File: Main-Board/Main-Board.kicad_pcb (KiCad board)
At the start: 2 copper layers, 50 x 50 mm, 68 parts, among them J1 Power_In, J2 ESC_1, J3 ESC_2, J4 ESC_3, J5 ESC_4, J6 Receiver, J7 Aux, J8 USB_B_Micro, J9 ICSP, Q1 BSS138, Q2 BSS138, SW1 Reset, U1 MCP6001U, U2 ICM-20689, U3 FT232RL, U4 ATmega328P-AU, U5 LM1117-5.0, Y1 16 MHz

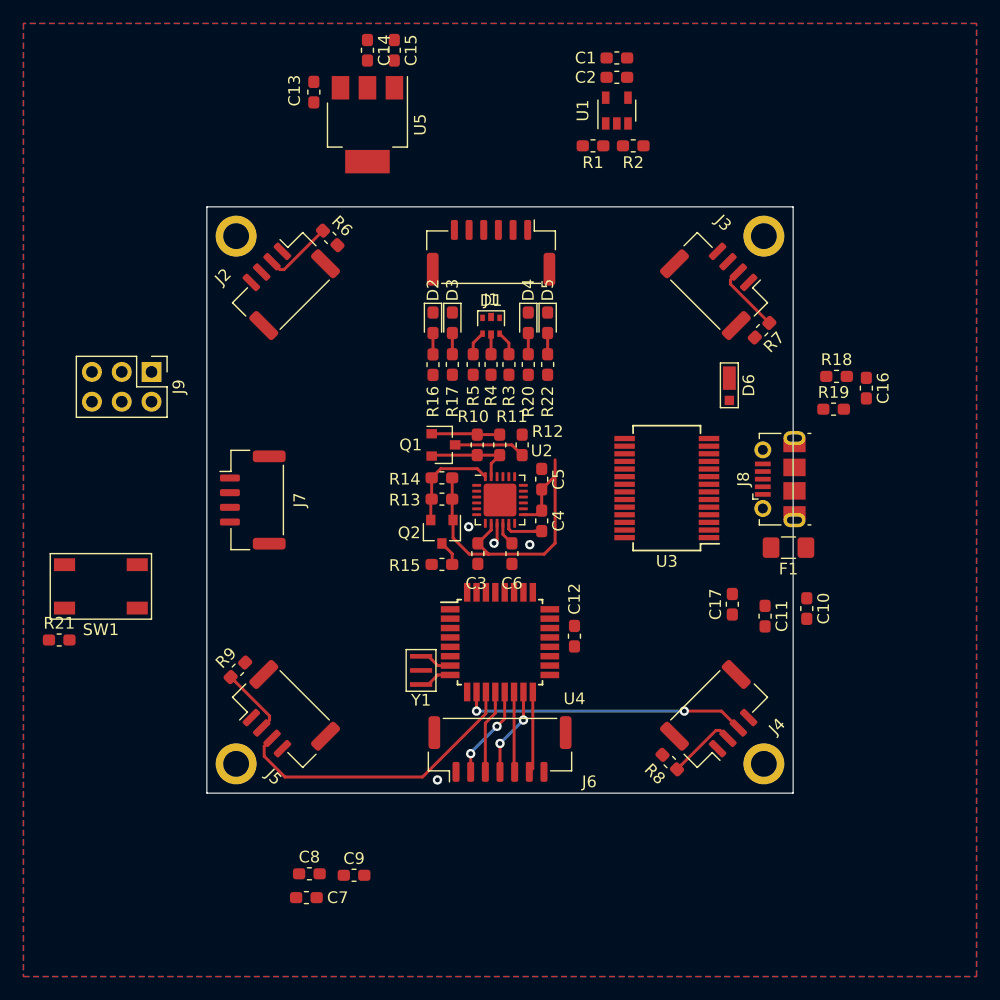
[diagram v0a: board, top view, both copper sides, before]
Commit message: 50% usb, ICSP, voltage monitoring, SDA/SCL, 48 tracks to go
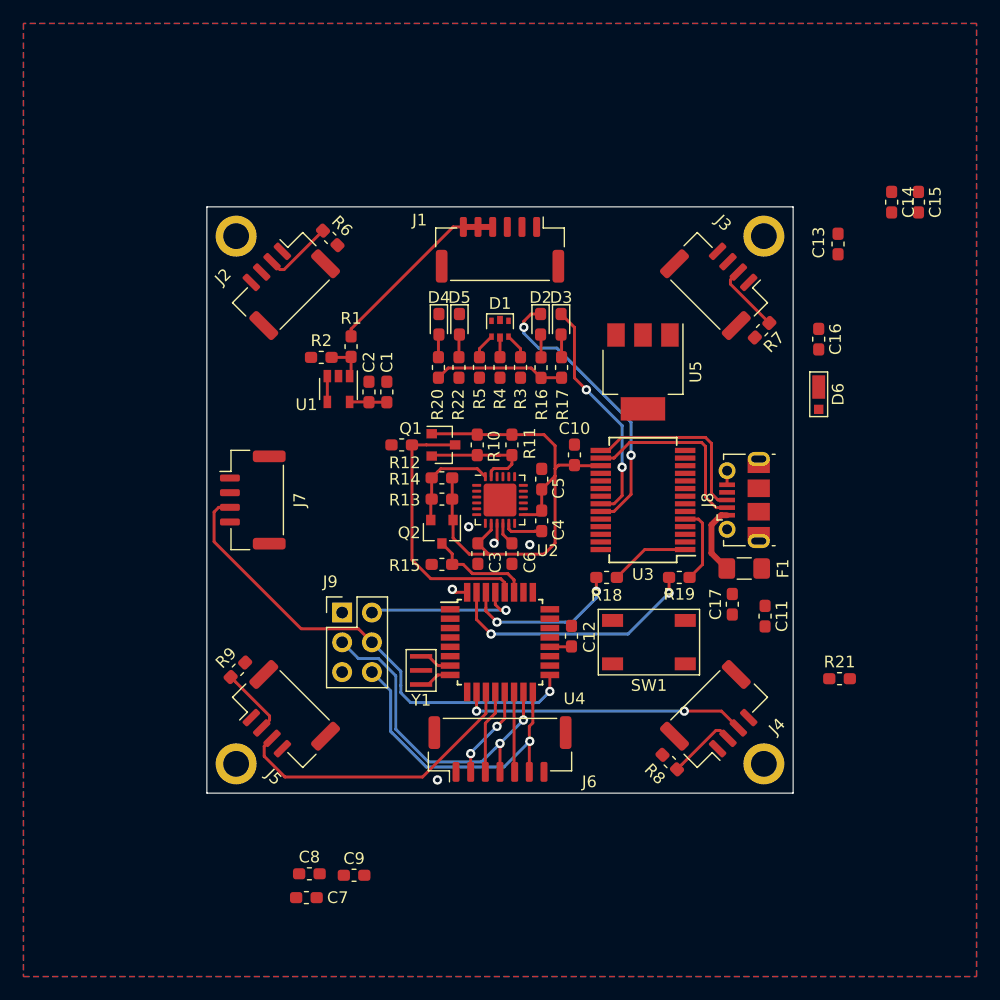
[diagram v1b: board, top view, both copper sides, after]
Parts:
- moved R21 66.6 mm to (117.9, 129.5)
- moved SW1 47.0 mm to (101.6, 126.4)
- moved C14 46.5 mm to (122.3, 88.9)
- moved C15 46.5 mm to (124.6, 88.9)
- moved C13 46.5 mm to (117.7, 92.5)
- moved C1 34.6 mm to (79.2, 105.1), turned to 270 degrees
- moved C2 34.2 mm to (77.7, 105.1), turned to 270 degrees
- moved U1 33.6 mm to (75.1, 104.8), turned to 270 degrees
- moved R2 32.1 mm to (73.7, 102.1), turned to 0 degrees
- moved U5 31.6 mm to (101.1, 103.4)
- moved R1 26.8 mm to (76.2, 101.2), turned to 90 degrees
- moved J9 26.2 mm to (75.4, 123.9), turned to 0 degrees
- moved R18 26.0 mm to (98.0, 120.9), turned to 180 degrees
- moved C10 23.8 mm to (95.2, 110.5), turned to 90 degrees
- moved R19 19.5 mm to (104.2, 120.9), turned to 180 degrees
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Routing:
- net Aux_Digital: track 0.00 -> 41.2 mm, vias 0 -> 1
- net Net-(D2-Pad1): track 0.00 -> 24.3 mm, vias 0 -> 2
- net Net-(R19-Pad2): track 0.00 -> 22.0 mm, vias 0 -> 2
- net D11: track 7.64 -> 28.7 mm
- net Net-(D3-Pad1): track 0.00 -> 19.8 mm, vias 0 -> 2
- net D12: track 6.94 -> 26.7 mm, vias 0 -> 1
- net A5_SCL: track 6.08 -> 23.0 mm
- net VDD: track 0.00 -> 16.3 mm
- net Net-(J8-Pad2): track 0.00 -> 16.1 mm
- net Net-(J8-Pad3): track 0.00 -> 15.9 mm
- net +5V: track 0.00 -> 14.4 mm
- net Net-(R18-Pad2): track 0.00 -> 14.0 mm, vias 0 -> 2
- net RESET: track 0.00 -> 13.7 mm, vias 0 -> 1
- net +3V3: track 36.4 -> 46.7 mm
- net A4_SDA: track 2.15 -> 9.03 mm
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
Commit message: USB and voltage regulator routed, all components are now on the board
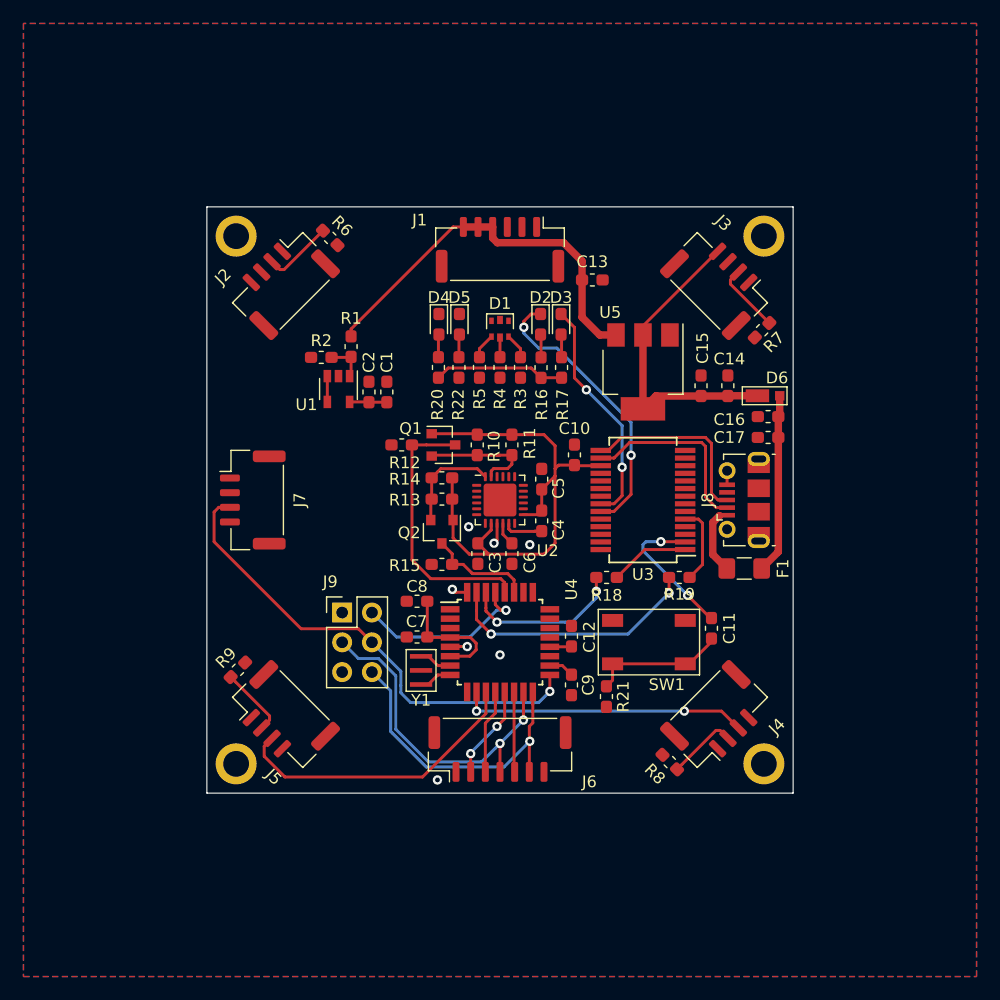
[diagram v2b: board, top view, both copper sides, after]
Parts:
- moved C8 25.0 mm to (81.8, 122.9), turned to 180 degrees
- moved C9 24.6 mm to (95.0, 130.1), turned to 270 degrees
- moved C15 24.3 mm to (106.0, 104.6), turned to 90 degrees
- moved C7 24.1 mm to (81.8, 126.0), turned to 0 degrees
- moved C13 21.2 mm to (96.8, 95.5), turned to 0 degrees
- moved C14 21.0 mm to (108.3, 104.6), turned to 90 degrees
- moved R21 19.9 mm to (98.0, 131.1), turned to 270 degrees
- moved C17 14.5 mm to (111.8, 109.0), turned to 180 degrees
- moved C16 7.89 mm to (111.8, 107.2), turned to 180 degrees
- moved C11 4.69 mm to (106.9, 125.2), turned to 90 degrees
- moved D6 4.01 mm to (112.1, 105.4), turned to 0 degrees
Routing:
- net +5V: track 14.4 -> 53.3 mm
- net VDD: track 16.3 -> 34.0 mm
- net VBUS: track 0.00 -> 15.4 mm
- net RESET: track 13.7 -> 27.3 mm
- net Net-(C11-Pad2): track 0.00 -> 12.4 mm, vias 0 -> 2
- net GND: track 6.39 -> 7.86 mm, vias 4 -> 6
- net Net-(F1-Pad1): track 5.93 -> 5.24 mm

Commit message: more routing, back up before fixing some errors
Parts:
- moved C14 12.7 mm to (95.8, 106.1), turned to 270 degrees
- moved C15 8.81 mm to (97.4, 106.1), turned to 270 degrees
- moved U5 0.76 mm to (101.9, 103.4)
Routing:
- net +5V: track 53.3 -> 216.4 mm, vias 0 -> 4
- net Aux_Digital: track 41.2 -> 68.9 mm, vias 1 -> 3
- net D2: track 1.37 -> 21.7 mm, vias 1 -> 2
- net Net-(C11-Pad2): track 12.4 -> 10.4 mm
- net B_RGB_LED: track 0.00 -> 1.26 mm, vias 0 -> 1
- net VDD: track 34.0 -> 34.8 mm
- net GND: vias 6 -> 11

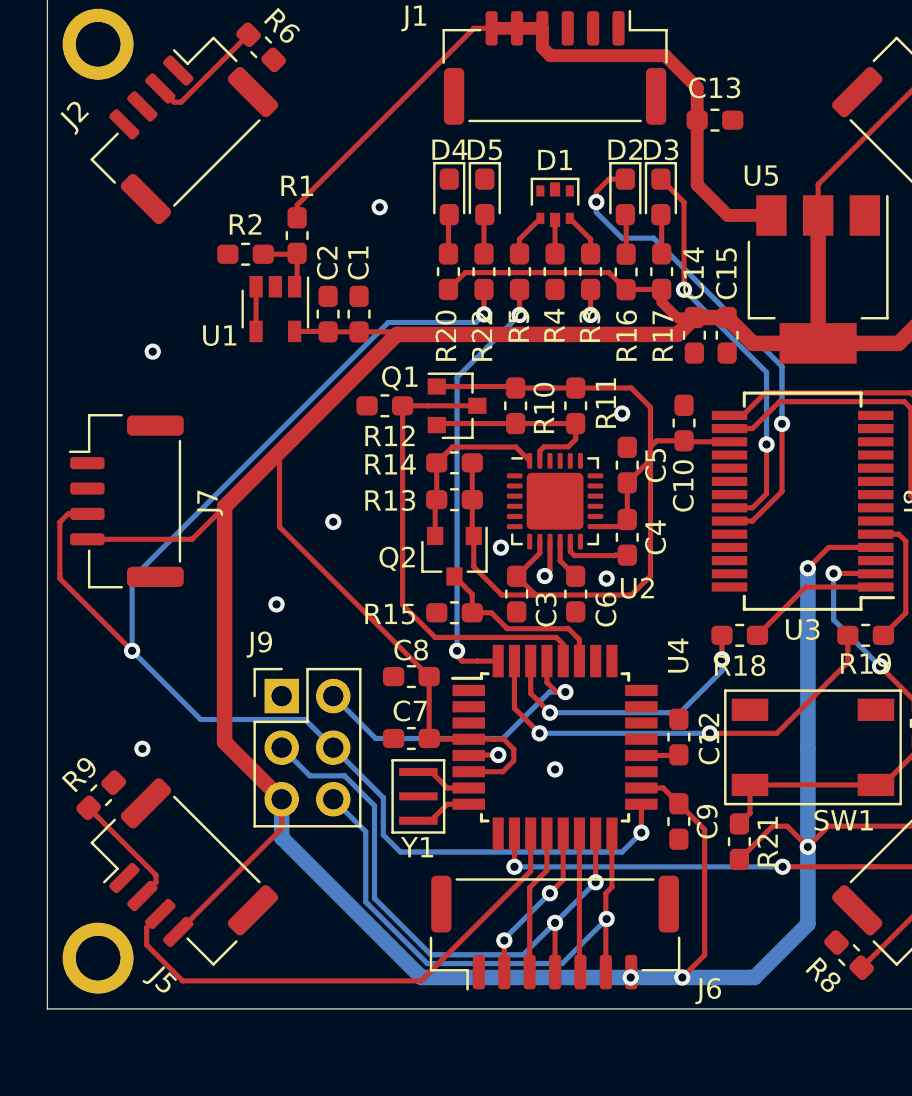
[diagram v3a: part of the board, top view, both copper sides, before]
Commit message: add attacheted lights to open ATMEGA ports (A4 cant be used again, dont mess with tx/rx) and removed 5th rc input. Add cap for USB
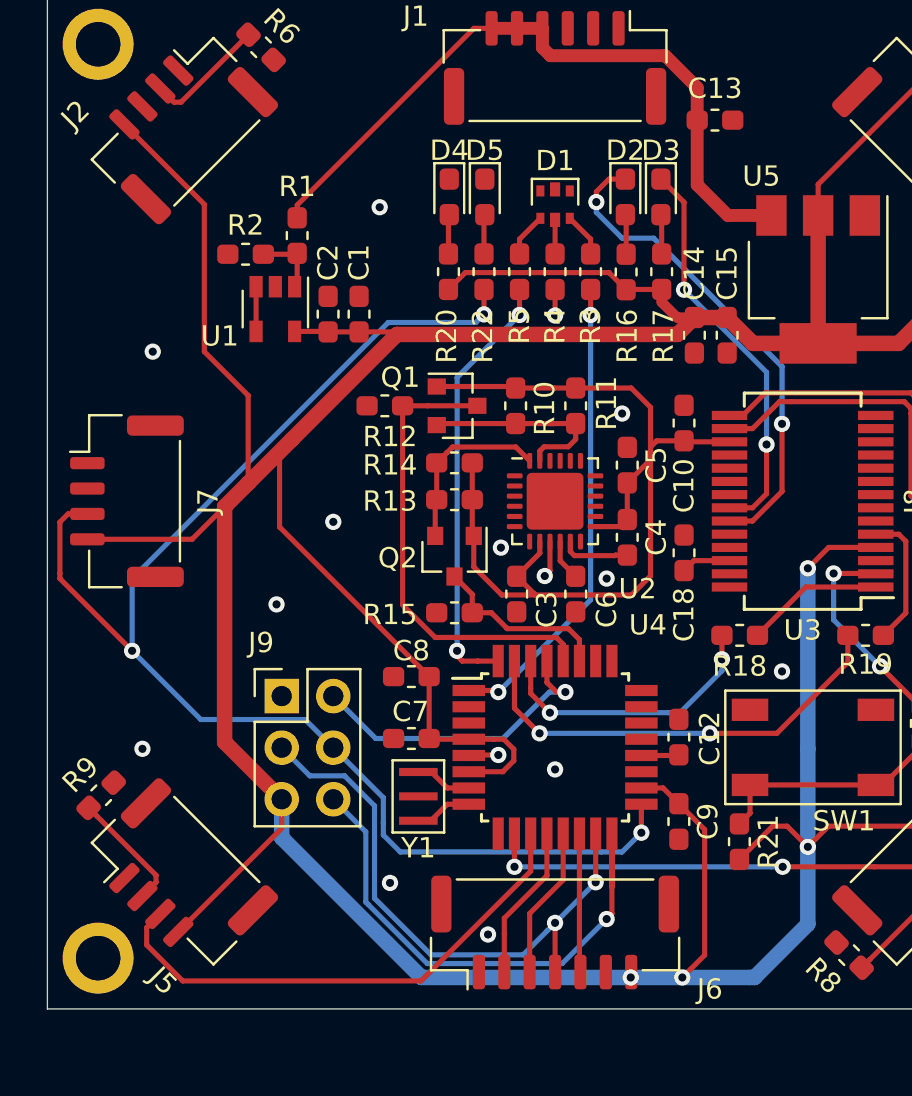
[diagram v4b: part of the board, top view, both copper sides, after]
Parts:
- added C18: 0.1uF 16V X7R 10%, Capacitor_SMD:C_0603_1608Metric_Pad1.05x0.95mm_HandSolder, F.Cu at (95.2, 116.8)
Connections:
- J6 pad 2: D9 -> D8
- J6 pad 3: D8 -> D9
- J6 pad 6: D12 -> (no net)
- R4 pad 1: (no net) -> D12
- R9 pad 1: (no net) -> A7
- U4 pad 22: (no net) -> A7
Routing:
- net B_RGB_LED: track 1.26 -> 23.2 mm, vias 1 -> 2
- net +5V: track 216.4 -> 236.6 mm
- net GND: track 7.86 -> 10.3 mm, vias 11 -> 14
- net D12: track 26.7 -> 28.0 mm, vias 1 -> 2
- net D8: track 7.17 -> 7.68 mm
- net D9: track 8.02 -> 7.50 mm, vias 2 -> 0

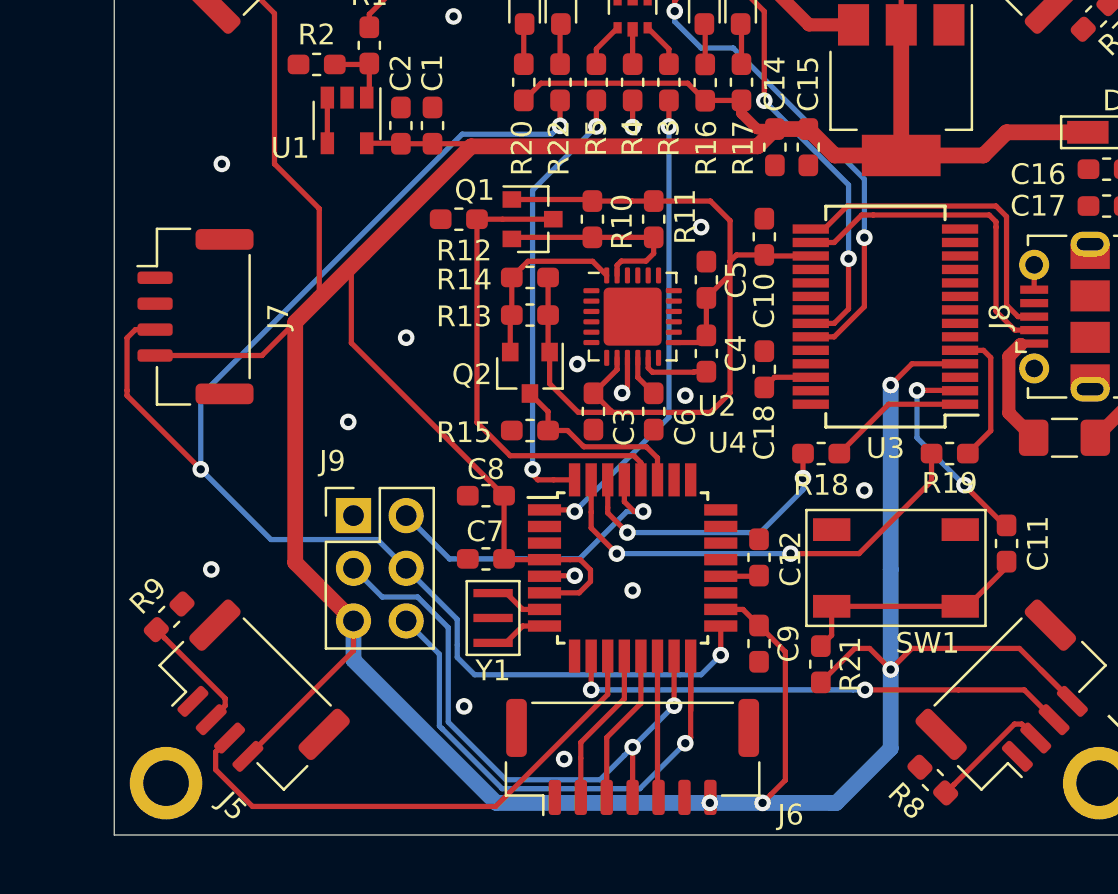
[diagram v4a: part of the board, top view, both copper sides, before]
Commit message: New schematic time... Switching to ATmega32U4
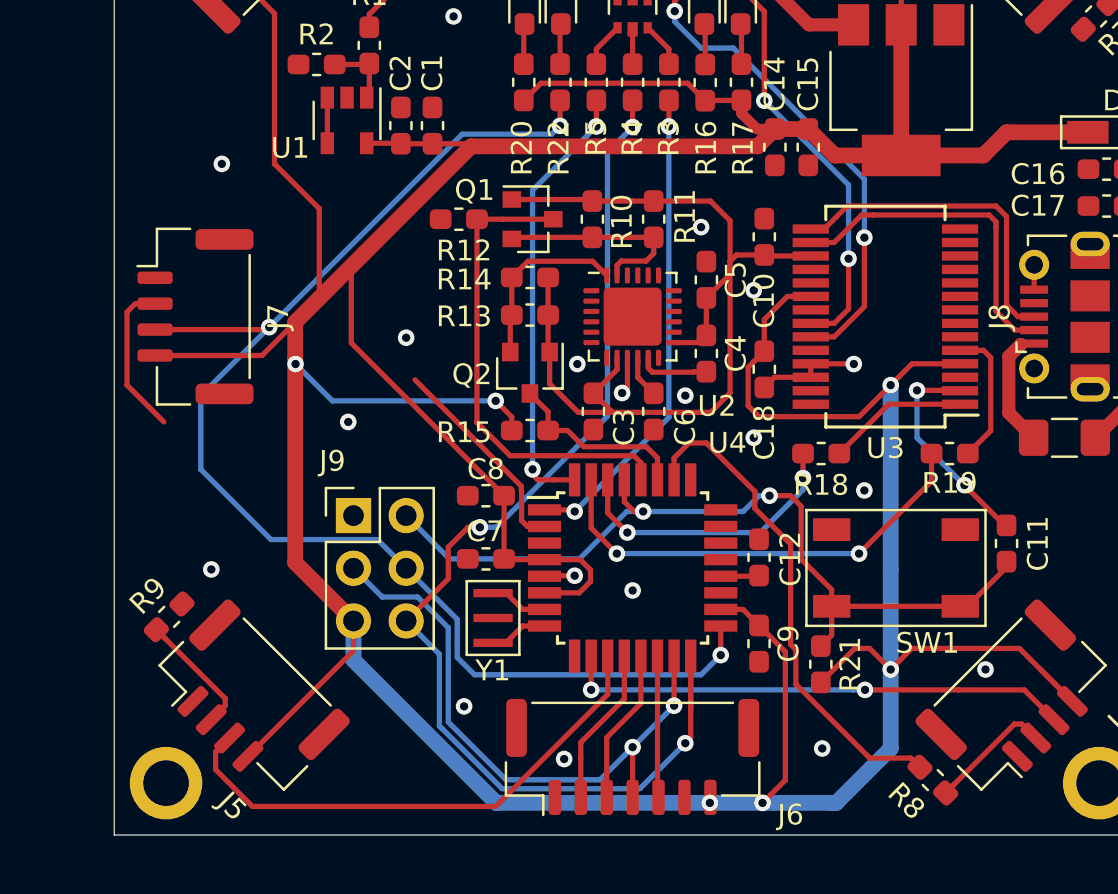
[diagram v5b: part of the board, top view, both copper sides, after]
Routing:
- net D12: track 28.0 -> 57.1 mm, vias 2 -> 3
- net +5V: track 236.6 -> 263.6 mm, vias 4 -> 6
- net A3: track 0.00 -> 24.0 mm
- net RESET: track 27.3 -> 40.9 mm, vias 1 -> 2
- net D4: track 0.00 -> 10.1 mm
- net A6: track 0.00 -> 7.56 mm
- net Aux_Digital: track 68.9 -> 65.1 mm
- net GND: track 10.3 -> 13.0 mm, vias 14 -> 19
